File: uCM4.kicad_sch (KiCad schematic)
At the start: 30 parts, among them J1 Conn_01x03, J2 Ethernet, J3 Micro_SD_Card, J4 USB_B_Micro, SW1 SW_DIP_x01, SW2 SW_DIP_x01, U1 RT9742GGJ5, U2 74LVC1G07, U3 TPD4EUSB30

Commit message: Update Ethernet on board
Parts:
- J2: footprint Connector_RJ:RJ45_UDE_RB1-125B8G1A -> Special:RB1-2S5BAK1A
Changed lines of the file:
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@@
     (property "Reference" "J2" (id 0) (at 144.145 32.1776 0))
     (property "Value" "Ethernet" (id 1) (at 144.145 34.4763 0))
-    (property "Footprint" "Connector_RJ:RJ45_UDE_RB1-125B8G1A" (id 2) (at 158.75 38.1 0)
+    (property "Footprint" "Special:RB1-2S5BAK1A" (id 2) (at 158.75 38.1 0)
       (effects (font (size 1.27 1.27)) hide)
     )
@@
     )
     (path "/04e34fb1-a3be-46e0-8875-d2b71b4b5a2a"
-      (reference "J2") (unit 1) (value "Ethernet") (footprint "Connector_RJ:RJ45_UDE_RB1-125B8G1A")
+      (reference "J2") (unit 1) (value "Ethernet") (footprint "Special:RB1-2S5BAK1A")
     )
     (path "/ae1796f2-3eee-4369-896e-b817a457af1e"

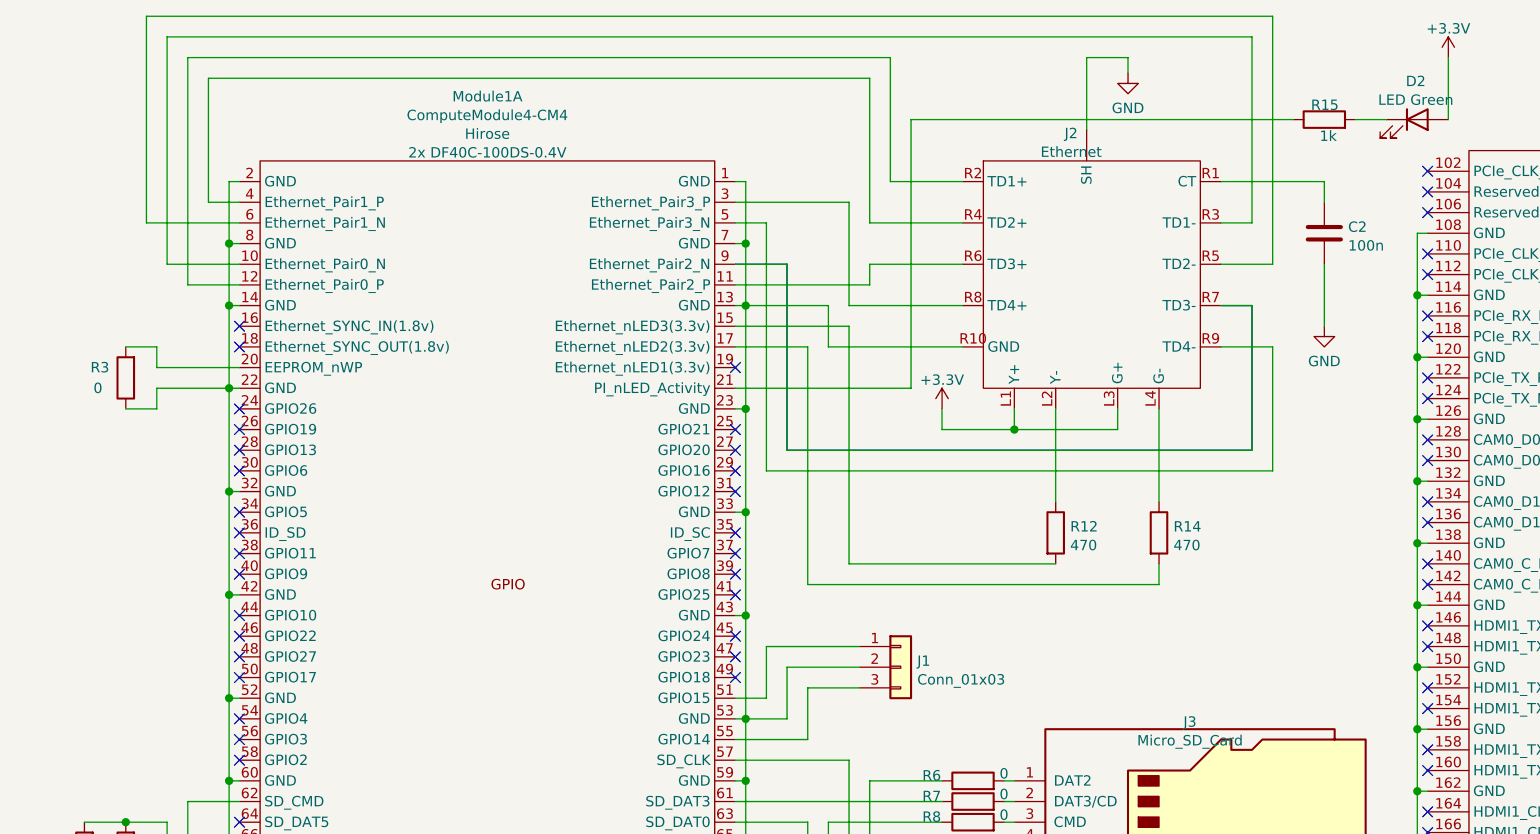
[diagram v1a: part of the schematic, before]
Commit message: Fix electrical connections of Eth
Old Ethernet connector had different pin meaning, despite almost same
footprint. Update schematics to match new connector.
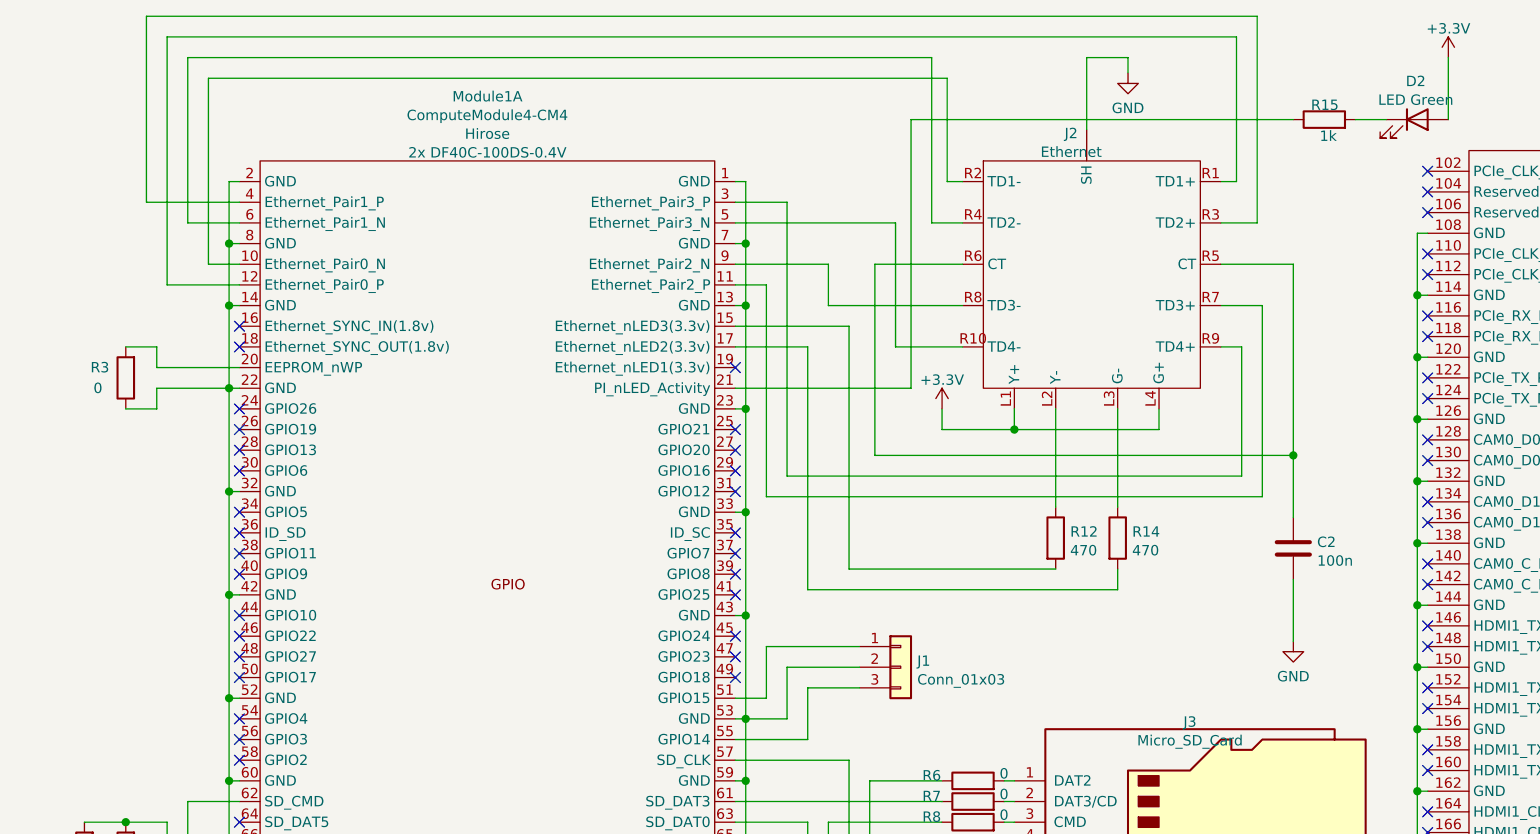
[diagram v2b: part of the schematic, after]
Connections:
- net +3V3: now also J2.L4 (G+); no longer J2.L3 (G+)
- net GND: no longer J2.R10 (GND)
- net at R14.1: now also J2.L3 (G-); no longer J2.L4 (G-)
- net at J2.R1 (TD1+): now also Module1.12 (Ethernet_Pair0_P); no longer C2.1
- net at J2.R2 (TD1-): now also Module1.10 (Ethernet_Pair0_N); no longer Module1.12 (Ethernet_Pair0_P)
- net at J2.R3 (TD2+): now also Module1.4 (Ethernet_Pair1_P); no longer Module1.10 (Ethernet_Pair0_N)
- net at J2.R4 (TD2-): now also Module1.6 (Ethernet_Pair1_N); no longer Module1.4 (Ethernet_Pair1_P)
- net at J2.R5 (CT): now also C2.1, J2.R6 (CT); no longer Module1.6 (Ethernet_Pair1_N)
- net at Module1.11 (Ethernet_Pair2_P): now also J2.R7 (TD3+); no longer J2.R6 (TD3+)
- net at Module1.9 (Ethernet_Pair2_N): now also J2.R8 (TD3-); no longer J2.R7 (TD3-)
- net at Module1.3 (Ethernet_Pair3_P): now also J2.R9 (TD4+); no longer J2.R8 (TD4+)
- net at Module1.5 (Ethernet_Pair3_N): now also J2.R10 (TD4-); no longer J2.R9 (TD4-)
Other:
- moved on the sheet: C2, R12, R14

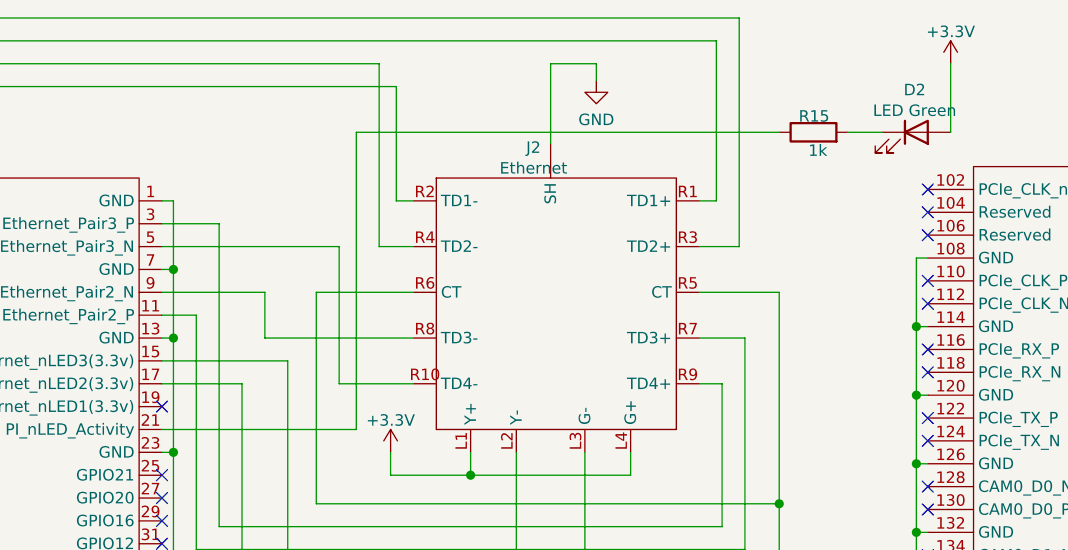
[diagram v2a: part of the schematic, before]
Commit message: Add net names for Ethernet
Is required to setup differential pairs.
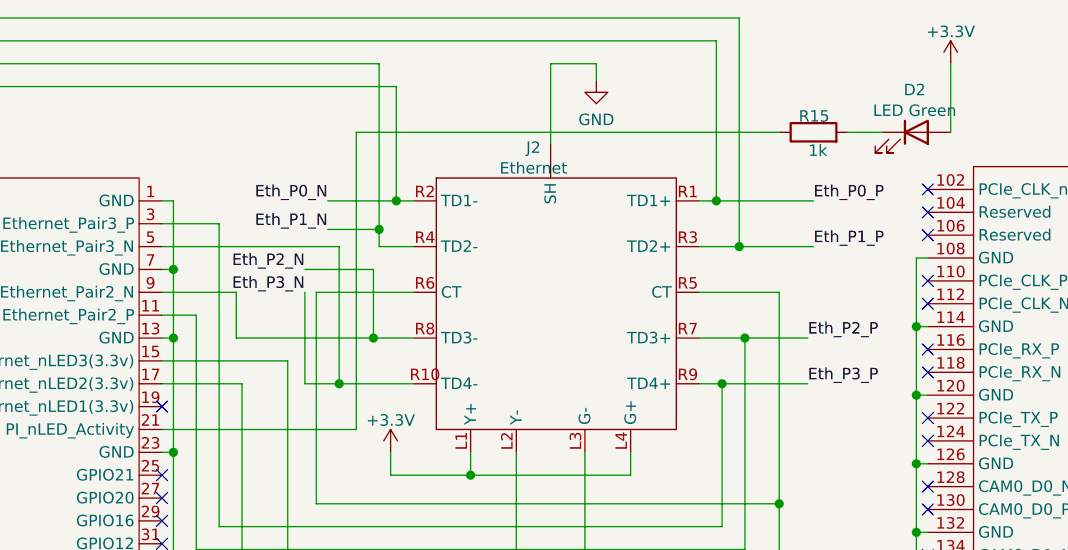
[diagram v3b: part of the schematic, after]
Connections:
- net Eth_P0_P: now reaches J2.R1 (TD1+), Module1.12 (Ethernet_Pair0_P)
- net Eth_P3_N: now reaches J2.R10 (TD4-), Module1.5 (Ethernet_Pair3_N)
- net Eth_P0_N: now reaches J2.R2 (TD1-), Module1.10 (Ethernet_Pair0_N)
- net Eth_P1_P: now reaches J2.R3 (TD2+), Module1.4 (Ethernet_Pair1_P)
- net Eth_P1_N: now reaches J2.R4 (TD2-), Module1.6 (Ethernet_Pair1_N)
- net Eth_P2_P: now reaches J2.R7 (TD3+), Module1.11 (Ethernet_Pair2_P)
- net Eth_P2_N: now reaches J2.R8 (TD3-), Module1.9 (Ethernet_Pair2_N)
- net Eth_P3_P: now reaches J2.R9 (TD4+), Module1.3 (Ethernet_Pair3_P)
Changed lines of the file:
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@@
   (junction (at 118.11 134.62) (diameter 1.016) (color 0 0 0 0))
   (junction (at 118.11 146.05) (diameter 1.016) (color 0 0 0 0))
+  (junction (at 122.555 58.42) (diameter 1.016) (color 0 0 0 0))
   (junction (at 124.46 152.4) (diameter 1.016) (color 0 0 0 0))
+  (junction (at 126.365 53.34) (diameter 1.016) (color 0 0 0 0))
+  (junction (at 127 41.275) (diameter 1.016) (color 0 0 0 0))
+  (junction (at 128.905 38.1) (diameter 1.016) (color 0 0 0 0))
   (junction (at 137.16 68.58) (diameter 1.016) (color 0 0 0 0))
+  (junction (at 164.465 38.1) (diameter 1.016) (color 0 0 0 0))
+  (junction (at 165.1 58.42) (diameter 1.016) (color 0 0 0 0))
+  (junction (at 167.005 43.18) (diameter 1.016) (color 0 0 0 0))
+  (junction (at 167.64 53.34) (diameter 1.016) (color 0 0 0 0))
   (junction (at 171.45 71.755) (diameter 1.016) (color 0 0 0 0))
   (junction (at 186.69 52.07) (diameter 1.016) (color 0 0 0 0))
@@
     (stroke (width 0) (type solid) (color 0 0 0 0))
   )
-  (wire (pts (xy 102.87 48.26) (xy 114.3 48.26))
+  (wire (pts (xy 102.87 48.26) (xy 111.125 48.26))
     (stroke (width 0) (type solid) (color 0 0 0 0))
   )
@@
     (stroke (width 0) (type solid) (color 0 0 0 0))
   )
+  (wire (pts (xy 111.125 48.26) (xy 111.125 53.34))
+    (stroke (width 0) (type solid) (color 0 0 0 0))
+  )
+  (wire (pts (xy 111.125 53.34) (xy 126.365 53.34))
+    (stroke (width 0) (type solid) (color 0 0 0 0))
+  )
   (wire (pts (xy 111.76 58.42) (xy 111.76 88.265))
     (stroke (width 0) (type solid) (color 0 0 0 0))
@@
     (stroke (width 0) (type solid) (color 0 0 0 0))
   )
-  (wire (pts (xy 114.3 48.26) (xy 114.3 53.34))
-    (stroke (width 0) (type solid) (color 0 0 0 0))
-  )
-  (wire (pts (xy 114.3 53.34) (xy 130.81 53.34))
-    (stroke (width 0) (type solid) (color 0 0 0 0))
-  )
   (wire (pts (xy 114.3 116.84) (xy 114.3 172.72))
     (stroke (width 0) (type solid) (color 0 0 0 0))
@@
     (stroke (width 0) (type solid) (color 0 0 0 0))
   )
+  (wire (pts (xy 118.745 45.72) (xy 126.365 45.72))
+    (stroke (width 0) (type solid) (color 0 0 0 0))
+  )
+  (wire (pts (xy 118.745 48.26) (xy 118.745 58.42))
+    (stroke (width 0) (type solid) (color 0 0 0 0))
+  )
+  (wire (pts (xy 118.745 58.42) (xy 122.555 58.42))
+    (stroke (width 0) (type solid) (color 0 0 0 0))
+  )
   (wire (pts (xy 119.38 111.76) (xy 119.38 124.46))
     (stroke (width 0) (type solid) (color 0 0 0 0))
@@
     (stroke (width 0) (type solid) (color 0 0 0 0))
   )
+  (wire (pts (xy 121.285 38.1) (xy 128.905 38.1))
+    (stroke (width 0) (type solid) (color 0 0 0 0))
+  )
+  (wire (pts (xy 121.285 41.275) (xy 127 41.275))
+    (stroke (width 0) (type solid) (color 0 0 0 0))
+  )
   (wire (pts (xy 121.92 124.46) (xy 137.16 124.46))
     (stroke (width 0) (type solid) (color 0 0 0 0))
@@
     (stroke (width 0) (type solid) (color 0 0 0 0))
   )
-  (wire (pts (xy 127 22.86) (xy 127 43.18))
+  (wire (pts (xy 126.365 45.72) (xy 126.365 53.34))
+    (stroke (width 0) (type solid) (color 0 0 0 0))
+  )
+  (wire (pts (xy 126.365 53.34) (xy 130.81 53.34))
+    (stroke (width 0) (type solid) (color 0 0 0 0))
+  )
+  (wire (pts (xy 127 22.86) (xy 127 41.275))
+    (stroke (width 0) (type solid) (color 0 0 0 0))
+  )
+  (wire (pts (xy 127 41.275) (xy 127 43.18))
     (stroke (width 0) (type solid) (color 0 0 0 0))
   )
@@
     (stroke (width 0) (type solid) (color 0 0 0 0))
   )
+  (wire (pts (xy 164.465 38.1) (xy 175.26 38.1))
+    (stroke (width 0) (type solid) (color 0 0 0 0))
+  )
   (wire (pts (xy 165.1 58.42) (xy 162.56 58.42))
     (stroke (width 0) (type solid) (color 0 0 0 0))
   )
+  (wire (pts (xy 165.1 58.42) (xy 174.625 58.42))
+    (stroke (width 0) (type solid) (color 0 0 0 0))
+  )
   (wire (pts (xy 165.1 74.295) (xy 165.1 58.42))
     (stroke (width 0) (type solid) (color 0 0 0 0))
@@
     (stroke (width 0) (type solid) (color 0 0 0 0))
   )
+  (wire (pts (xy 167.005 43.18) (xy 175.26 43.18))
+    (stroke (width 0) (type solid) (color 0 0 0 0))
+  )
   (wire (pts (xy 167.64 53.34) (xy 162.56 53.34))
+    (stroke (width 0) (type solid) (color 0 0 0 0))
+  )
+  (wire (pts (xy 167.64 53.34) (xy 174.625 53.34))
     (stroke (width 0) (type solid) (color 0 0 0 0))
   )
@@
     (effects (font (size 1.27 1.27)) (justify right bottom))
   )
+  (label "Eth_P2_N" (at 118.745 45.72 180)
+    (effects (font (size 1.27 1.27)) (justify right bottom))
+  )
+  (label "Eth_P3_N" (at 118.745 48.26 180)
+    (effects (font (size 1.27 1.27)) (justify right bottom))
+  )
+  (label "Eth_P0_N" (at 121.285 38.1 180)
+    (effects (font (size 1.27 1.27)) (justify right bottom))
+  )
+  (label "Eth_P1_N" (at 121.285 41.275 180)
+    (effects (font (size 1.27 1.27)) (justify right bottom))
+  )
+  (label "Eth_P2_P" (at 174.625 53.34 0)
+    (effects (font (size 1.27 1.27)) (justify left bottom))
+  )
+  (label "Eth_P3_P" (at 174.625 58.42 0)
+    (effects (font (size 1.27 1.27)) (justify left bottom))
+  )
+  (label "Eth_P0_P" (at 175.26 38.1 0)
+    (effects (font (size 1.27 1.27)) (justify left bottom))
+  )
+  (label "Eth_P1_P" (at 175.26 43.18 0)
+    (effects (font (size 1.27 1.27)) (justify left bottom))
+  )
   (global_label "TODO" (shape input) (at 41.91 137.16 180)

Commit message: Make USB differential
Rename net to allow differential routing
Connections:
- net USB_N: now reaches J4.2 (D-), Module1.103 (USB2_N), U3.1 (D1+)
- net USB_P: now reaches J4.3 (D+), Module1.105 (USB2_P), U3.2 (D1-)
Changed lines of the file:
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@@
   (junction (at 250.19 151.13) (diameter 1.016) (color 0 0 0 0))
   (junction (at 250.19 158.75) (diameter 1.016) (color 0 0 0 0))
+  (junction (at 250.825 39.37) (diameter 1.016) (color 0 0 0 0))
   (junction (at 252.73 41.91) (diameter 1.016) (color 0 0 0 0))
   (junction (at 255.27 39.37) (diameter 1.016) (color 0 0 0 0))
@@
     (stroke (width 0) (type solid) (color 0 0 0 0))
   )
-  (wire (pts (xy 248.92 39.37) (xy 255.27 39.37))
+  (wire (pts (xy 248.92 39.37) (xy 250.825 39.37))
     (stroke (width 0) (type solid) (color 0 0 0 0))
   )
@@
     (stroke (width 0) (type solid) (color 0 0 0 0))
   )
+  (wire (pts (xy 250.825 26.035) (xy 250.825 39.37))
+    (stroke (width 0) (type solid) (color 0 0 0 0))
+  )
+  (wire (pts (xy 250.825 39.37) (xy 255.27 39.37))
+    (stroke (width 0) (type solid) (color 0 0 0 0))
+  )
+  (wire (pts (xy 252.73 29.21) (xy 252.73 41.91))
+    (stroke (width 0) (type solid) (color 0 0 0 0))
+  )
   (wire (pts (xy 252.73 41.91) (xy 252.73 71.12))
     (stroke (width 0) (type solid) (color 0 0 0 0))
@@
   )
   (wire (pts (xy 254 161.29) (xy 254 158.75))
+    (stroke (width 0) (type solid) (color 0 0 0 0))
+  )
+  (wire (pts (xy 255.27 26.035) (xy 250.825 26.035))
+    (stroke (width 0) (type solid) (color 0 0 0 0))
+  )
+  (wire (pts (xy 255.27 29.21) (xy 252.73 29.21))
     (stroke (width 0) (type solid) (color 0 0 0 0))
   )
@@
     (effects (font (size 1.27 1.27)) (justify left bottom))
   )
+  (label "USB_N" (at 255.27 26.035 0)
+    (effects (font (size 1.27 1.27)) (justify left bottom))
+  )
+  (label "USB_P" (at 255.27 29.21 0)
+    (effects (font (size 1.27 1.27)) (justify left bottom))
+  )

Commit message: Name some signals on schematics
Makes reading PCB easier.
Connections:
- net PowerOn: now reaches Module1.99 (Global_EN), SW2.2
- net RESET: now reaches Module1.92 (RUN_PG), SW1.2
- net RX: now reaches J1.1 (Pin_1), Module1.51 (GPIO15)
- net TX: now reaches J1.3 (Pin_3), Module1.55 (GPIO14)
- net SD_EN: now reaches Module1.75 (SD_PWR_ON), R5.1, U1.4 (EN)
- net SD_PWR: now reaches C1.2, J3.4 (VDD), U1.1 (OUT)
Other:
- note removed: "POWER ON"
- note removed: "RESET"
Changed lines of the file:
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@@
   (junction (at 27.94 116.84) (diameter 1.016) (color 0 0 0 0))
   (junction (at 31.75 142.24) (diameter 1.016) (color 0 0 0 0))
+  (junction (at 32.385 152.4) (diameter 1.016) (color 0 0 0 0))
   (junction (at 40.64 45.72) (diameter 1.016) (color 0 0 0 0))
   (junction (at 40.64 53.34) (diameter 1.016) (color 0 0 0 0))
@@
   (junction (at 104.14 119.38) (diameter 1.016) (color 0 0 0 0))
   (junction (at 104.14 127) (diameter 1.016) (color 0 0 0 0))
+  (junction (at 106.68 95.25) (diameter 1.016) (color 0 0 0 0))
   (junction (at 109.22 132.08) (diameter 1.016) (color 0 0 0 0))
+  (junction (at 111.76 106.68) (diameter 1.016) (color 0 0 0 0))
+  (junction (at 111.76 177.8) (diameter 1.016) (color 0 0 0 0))
   (junction (at 118.11 134.62) (diameter 1.016) (color 0 0 0 0))
   (junction (at 118.11 146.05) (diameter 1.016) (color 0 0 0 0))
@@
   (junction (at 126.365 53.34) (diameter 1.016) (color 0 0 0 0))
   (junction (at 127 41.275) (diameter 1.016) (color 0 0 0 0))
+  (junction (at 127 134.62) (diameter 1.016) (color 0 0 0 0))
   (junction (at 128.905 38.1) (diameter 1.016) (color 0 0 0 0))
   (junction (at 137.16 68.58) (diameter 1.016) (color 0 0 0 0))
+  (junction (at 146.05 152.4) (diameter 1.016) (color 0 0 0 0))
   (junction (at 164.465 38.1) (diameter 1.016) (color 0 0 0 0))
   (junction (at 165.1 58.42) (diameter 1.016) (color 0 0 0 0))
@@
   (no_connect (at 280.67 66.04))
   (no_connect (at 280.67 71.12))
-  (wire (pts (xy 16.51 152.4) (xy 41.91 152.4))
+  (wire (pts (xy 16.51 152.4) (xy 32.385 152.4))
     (stroke (width 0) (type solid) (color 0 0 0 0))
   )
@@
     (stroke (width 0) (type solid) (color 0 0 0 0))
   )
+  (wire (pts (xy 26.67 156.21) (xy 32.385 156.21))
+    (stroke (width 0) (type solid) (color 0 0 0 0))
+  )
   (wire (pts (xy 27.94 124.46) (xy 27.94 142.24))
     (stroke (width 0) (type solid) (color 0 0 0 0))
@@
     (stroke (width 0) (type solid) (color 0 0 0 0))
   )
+  (wire (pts (xy 32.385 152.4) (xy 41.91 152.4))
+    (stroke (width 0) (type solid) (color 0 0 0 0))
+  )
+  (wire (pts (xy 32.385 156.21) (xy 32.385 152.4))
+    (stroke (width 0) (type solid) (color 0 0 0 0))
+  )
   (wire (pts (xy 33.02 20.32) (xy 33.02 50.8))
     (stroke (width 0) (type solid) (color 0 0 0 0))
@@
     (stroke (width 0) (type solid) (color 0 0 0 0))
   )
+  (wire (pts (xy 106.045 177.8) (xy 111.76 177.8))
+    (stroke (width 0) (type solid) (color 0 0 0 0))
+  )
   (wire (pts (xy 106.68 50.8) (xy 106.68 76.835))
     (stroke (width 0) (type solid) (color 0 0 0 0))
@@
     (stroke (width 0) (type solid) (color 0 0 0 0))
   )
+  (wire (pts (xy 106.68 92.71) (xy 106.68 95.25))
+    (stroke (width 0) (type solid) (color 0 0 0 0))
+  )
   (wire (pts (xy 106.68 95.25) (xy 118.11 95.25))
     (stroke (width 0) (type solid) (color 0 0 0 0))
@@
     (stroke (width 0) (type solid) (color 0 0 0 0))
   )
+  (wire (pts (xy 111.76 106.68) (xy 119.38 106.68))
+    (stroke (width 0) (type solid) (color 0 0 0 0))
+  )
   (wire (pts (xy 111.76 116.84) (xy 102.87 116.84))
     (stroke (width 0) (type solid) (color 0 0 0 0))
@@
     (stroke (width 0) (type solid) (color 0 0 0 0))
   )
+  (wire (pts (xy 119.38 92.71) (xy 106.68 92.71))
+    (stroke (width 0) (type solid) (color 0 0 0 0))
+  )
   (wire (pts (xy 119.38 111.76) (xy 119.38 124.46))
     (stroke (width 0) (type solid) (color 0 0 0 0))
@@
     (stroke (width 0) (type solid) (color 0 0 0 0))
   )
+  (wire (pts (xy 127 134.62) (xy 128.27 134.62))
+    (stroke (width 0) (type solid) (color 0 0 0 0))
+  )
   (wire (pts (xy 128.27 66.04) (xy 128.27 68.58))
     (stroke (width 0) (type solid) (color 0 0 0 0))
@@
   )
   (wire (pts (xy 146.05 146.05) (xy 146.05 152.4))
+    (stroke (width 0) (type solid) (color 0 0 0 0))
+  )
+  (wire (pts (xy 146.05 155.575) (xy 146.05 152.4))
     (stroke (width 0) (type solid) (color 0 0 0 0))
   )
@@
     (effects (font (size 1.27 1.27)) (justify right bottom))
   )
-  (text "RESET" (at 26.67 156.21 180)
+  (label "RESET" (at 26.67 156.21 180)
     (effects (font (size 1.27 1.27)) (justify right bottom))
   )
-  (text "POWER ON" (at 130.81 184.15 180)
+  (label "PowerOn" (at 106.045 177.8 180)
     (effects (font (size 1.27 1.27)) (justify right bottom))
   )
@@
     (effects (font (size 1.27 1.27)) (justify right bottom))
   )
+  (label "RX" (at 119.38 92.71 0)
+    (effects (font (size 1.27 1.27)) (justify left bottom))
+  )
+  (label "TX" (at 119.38 106.68 0)
+    (effects (font (size 1.27 1.27)) (justify left bottom))
+  )
   (label "Eth_P0_N" (at 121.285 38.1 180)
     (effects (font (size 1.27 1.27)) (justify right bottom))
@@
     (effects (font (size 1.27 1.27)) (justify right bottom))
   )
+  (label "SD_EN" (at 128.27 134.62 0)
+    (effects (font (size 1.27 1.27)) (justify left bottom))
+  )
+  (label "SD_PWR" (at 146.05 155.575 0)
+    (effects (font (size 1.27 1.27)) (justify left bottom))
+  )
   (label "Eth_P2_P" (at 174.625 53.34 0)
